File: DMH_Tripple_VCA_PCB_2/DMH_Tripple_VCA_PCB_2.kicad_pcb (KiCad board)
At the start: 2 copper layers, 48 x 175 mm, 0 parts

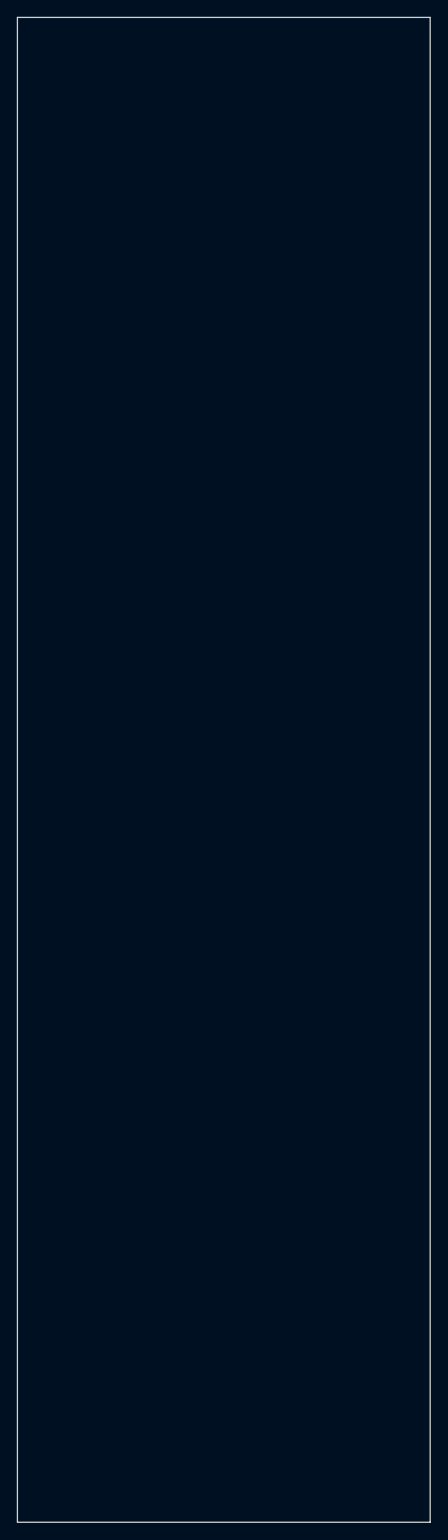
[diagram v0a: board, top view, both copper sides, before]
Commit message: Corrected header locations and placed pcb2 comps
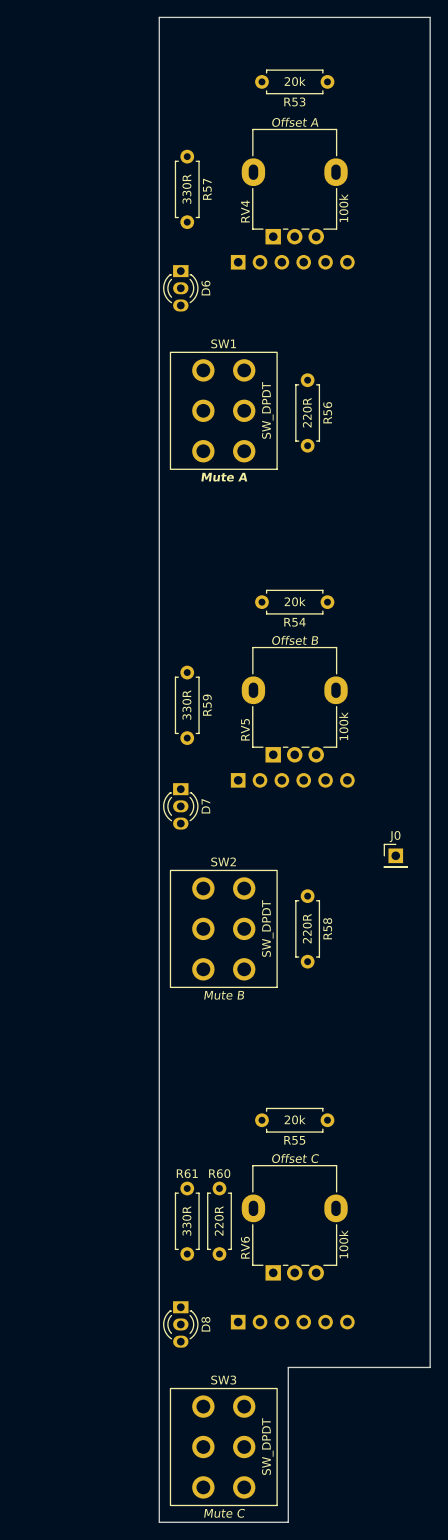
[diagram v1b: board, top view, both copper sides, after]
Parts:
- added D6: LED_Dual_AKA, SynthStuff:LED_D3.0mm-2color, F.Cu at (70.0, 74.0)
- added D7: LED_Dual_AKA, SynthStuff:LED_D3.0mm-2color, F.Cu at (70.0, 134.2)
- added D8: LED_Dual_AKA, SynthStuff:LED_D3.0mm-2color, F.Cu at (70.0, 194.5)
- added J0: Conn_01x01, Connector_PinHeader_2.54mm:PinHeader_1x01_P2.54mm_Vertical, F.Cu at (95.0, 140.0)
- added J50: Conn_01x06, Connector_PinHeader_2.54mm:PinHeader_1x06_P2.54mm_Vertical, B.Cu at (76.7, 71.0)
- added J60: Conn_01x06, Connector_PinHeader_2.54mm:PinHeader_1x06_P2.54mm_Vertical, B.Cu at (76.7, 131.2)
- added J70: Conn_01x06, Connector_PinHeader_2.54mm:PinHeader_1x06_P2.54mm_Vertical, B.Cu at (76.7, 194.2)
- added R53: 20k, Resistor_THT:R_Axial_DIN0207_L6.3mm_D2.5mm_P7.62mm_Horizontal, F.Cu at (87.1, 50.0)
- added R54: 20k, Resistor_THT:R_Axial_DIN0207_L6.3mm_D2.5mm_P7.62mm_Horizontal, F.Cu at (87.1, 110.5)
- added R55: 20k, Resistor_THT:R_Axial_DIN0207_L6.3mm_D2.5mm_P7.62mm_Horizontal, F.Cu at (87.1, 170.8)
- added R56: 220R, Resistor_THT:R_Axial_DIN0207_L6.3mm_D2.5mm_P7.62mm_Horizontal, F.Cu at (84.8, 84.7)
- added R57: 330R, Resistor_THT:R_Axial_DIN0207_L6.3mm_D2.5mm_P7.62mm_Horizontal, F.Cu at (70.8, 58.7)
- added R58: 220R, Resistor_THT:R_Axial_DIN0207_L6.3mm_D2.5mm_P7.62mm_Horizontal, F.Cu at (84.8, 144.7)
- added R59: 330R, Resistor_THT:R_Axial_DIN0207_L6.3mm_D2.5mm_P7.62mm_Horizontal, F.Cu at (70.8, 118.7)
- added R60: 220R, Resistor_THT:R_Axial_DIN0207_L6.3mm_D2.5mm_P7.62mm_Horizontal, F.Cu at (74.5, 178.7)
- added R61: 330R, Resistor_THT:R_Axial_DIN0207_L6.3mm_D2.5mm_P7.62mm_Horizontal, F.Cu at (70.8, 178.7)
- added RV4: 100k, SynthStuff:Potentiometer_Alpha_RD901F-40-00D_Single_Vertical, F.Cu at (80.8, 68.0)
- added RV5: 100k, SynthStuff:Potentiometer_Alpha_RD901F-40-00D_Single_Vertical, F.Cu at (80.8, 128.2)
- added RV6: 100k, SynthStuff:Potentiometer_Alpha_RD901F-40-00D_Single_Vertical, F.Cu at (80.8, 188.5)
- added SW1: SW_DPDT, SynthStuff:Toggle_Switch_2_Poles_THT, F.Cu at (75.0, 88.2)
- added SW2: SW_DPDT, SynthStuff:Toggle_Switch_2_Poles_THT, F.Cu at (75.0, 148.5)
- added SW3: SW_DPDT, SynthStuff:Toggle_Switch_2_Poles_THT, F.Cu at (75.0, 208.8)
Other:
- board size 48 x 175 mm -> 31.5 x 175 mm

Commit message: Routed PCB 2
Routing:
- net +12V: track 0.00 -> 173.6 mm
- net Net-(R60-Pad2): track 0.00 -> 29.2 mm
- net Net-(R53-Pad1): track 0.00 -> 20.6 mm
- net Net-(D8-A2): track 0.00 -> 20.6 mm
- net Net-(R55-Pad1): track 0.00 -> 20.4 mm
- net Net-(R54-Pad1): track 0.00 -> 20.4 mm
- net /Inputs and Outputs/Output B Jack: track 0.00 -> 19.1 mm
- net /Inputs and Outputs/Output A Jack: track 0.00 -> 19.1 mm
- net Net-(R61-Pad2): track 0.00 -> 18.5 mm
- net Net-(D6-A2): track 0.00 -> 18.3 mm
- net Net-(R59-Pad2): track 0.00 -> 18.3 mm
- net Net-(D7-A2): track 0.00 -> 18.2 mm
- net Net-(R57-Pad2): track 0.00 -> 18.0 mm
- net /Inputs and Outputs/Output C Jack: track 0.00 -> 16.3 mm
- net Net-(D8-A1): track 0.00 -> 14.5 mm
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- added copper zone on B.Cu, net GND
- added copper zone on F.Cu, net GND

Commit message: Generated Gerbers
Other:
- board text added: "Mk1.0 - March 2025"
- board text removed: "Mk1.0 - Month Year"
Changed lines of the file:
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@@
 			(plot_on_all_layers_selection 0x00000000_00000000_00000000_00000000)
 			(disableapertmacros no)
-			(usegerberextensions no)
+			(usegerberextensions yes)
 			(usegerberattributes yes)
 			(usegerberadvancedattributes yes)
@@
 			(sketchdnponfab yes)
 			(crossoutdnponfab yes)
-			(subtractmaskfromsilk no)
+			(subtractmaskfromsilk yes)
 			(outputformat 1)
 			(mirror no)
-			(drillshape 1)
+			(drillshape 0)
 			(scaleselection 1)
-			(outputdirectory "")
+			(outputdirectory "Gerbers/")
 		)
 	)
@@
 	)
 	(gr_rect
-		(start 94 186.25)
-		(end 96 196.25)
+		(start 94 186)
+		(end 96 196)
 		(stroke
 			(width 0.1)
@@
 		(layer "User.9")
 	)
-	(gr_text "Mk1.0 - Month Year"
-		(at 97.75 191.25 90)
+	(gr_text "Mk1.0 - March 2025"
+		(at 97.75 191 90)
 		(layer "B.SilkS")
 		(effects

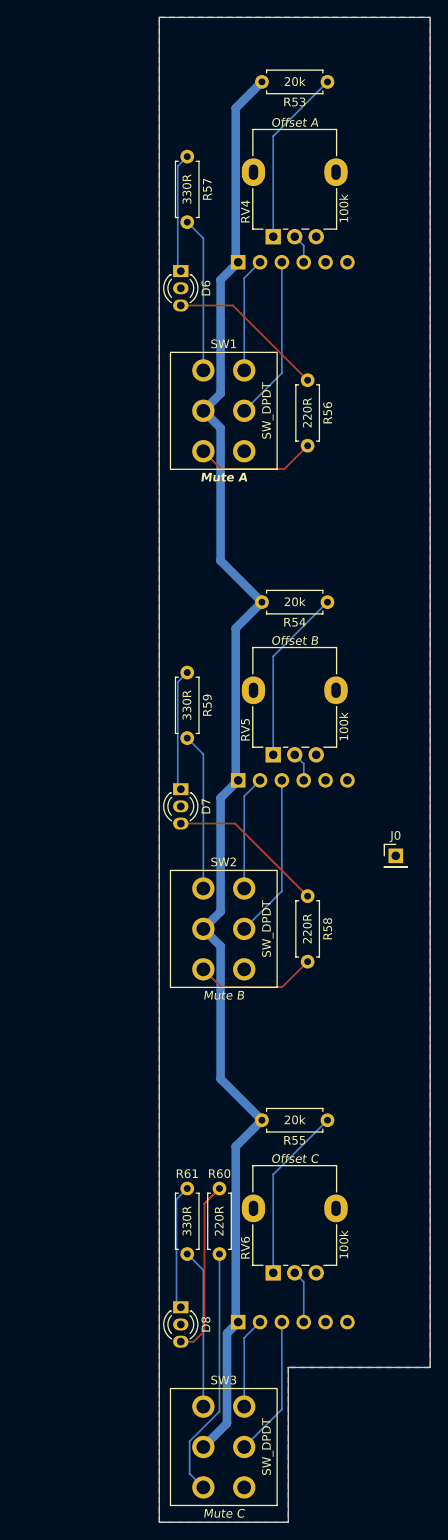
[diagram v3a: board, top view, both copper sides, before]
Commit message: Fixed mistakes in PCB 2
- Inverted offset potentiometers pinout
- LED resistors were too low, changed to 1k both colors
- Regenerated PCB 2 gerbers accordingly
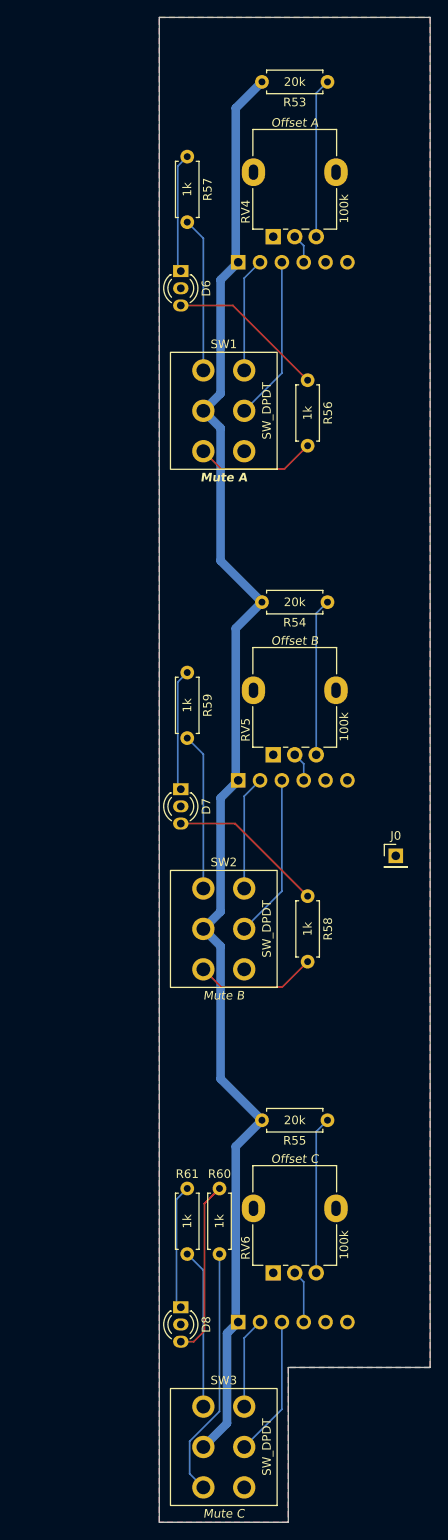
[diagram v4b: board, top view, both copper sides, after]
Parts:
- R56, R58, R60: value 220R -> 1k
- R57, R59, R61: value 330R -> 1k
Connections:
- RV4 pad 1: Net-(R53-Pad1) -> GND
- RV4 pad 3: GND -> Net-(R53-Pad1)
- RV5 pad 1: Net-(R54-Pad1) -> GND
- RV5 pad 3: GND -> Net-(R54-Pad1)
- RV6 pad 1: Net-(R55-Pad1) -> GND
- RV6 pad 3: GND -> Net-(R55-Pad1)
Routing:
- net Net-(R55-Pad1): track 20.4 -> 18.3 mm
- net Net-(R54-Pad1): track 20.4 -> 18.3 mm
- net Net-(R53-Pad1): track 20.6 -> 18.5 mm
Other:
- board text added: "Mk1.1 - March 2025"
- board text removed: "Mk1.0 - March 2025"
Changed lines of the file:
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@@
 			(layers "*.Cu" "*.Mask")
 			(remove_unused_layers no)
-			(net 20 "Net-(R55-Pad1)")
+			(net 3 "GND")
 			(pinfunction "1")
 			(pintype "passive")
@@
 			(layers "*.Cu" "*.Mask")
 			(remove_unused_layers no)
-			(net 3 "GND")
+			(net 20 "Net-(R55-Pad1)")
 			(pinfunction "3")
 			(pintype "passive")
@@
 			)
 		)
-		(property "Value" "330R"
+		(property "Value" "1k"
 			(at 3.81 0 90)
 			(layer "F.SilkS")
@@
 			)
 		)
-		(property "Value" "330R"
+		(property "Value" "1k"
 			(at 3.81 0 90)
 			(layer "F.SilkS")
@@
 			)
 		)
+		(property "Function" ""
+			(at 0 0 270)
+			(unlocked yes)
+			(layer "F.Fab")
+			(hide yes)
+			(effects
+				(font
+					(size 1 1)
+					(thickness 0.15)
+				)
+			)
+		)
 		(property ki_fp_filters "R_*")
 		(sheetname "/Inputs and Outputs/")
@@
 			)
 		)
-		(property "Value" "220R"
+		(property "Value" "1k"
 			(at 3.81 0 90)
 			(layer "F.SilkS")
@@
 			)
 		)
+		(property "Function" ""
+			(at 0 0 270)
+			(unlocked yes)
+			(layer "F.Fab")
+			(hide yes)
+			(effects
+				(font
+					(size 1 1)
+					(thickness 0.15)
+				)
+			)
+		)
 		(property ki_fp_filters "R_*")
 		(sheetname "/Inputs and Outputs/")
@@
 			(layers "*.Cu" "*.Mask")
 			(remove_unused_layers no)
-			(net 18 "Net-(R53-Pad1)")
+			(net 3 "GND")
 			(pinfunction "1")
 			(pintype "passive")
@@
 			(layers "*.Cu" "*.Mask")
 			(remove_unused_layers no)
-			(net 3 "GND")
+			(net 18 "Net-(R53-Pad1)")
 			(pinfunction "3")
 			(pintype "passive")
@@
 			)
 		)
-		(property "Value" "330R"
+		(property "Value" "1k"
 			(at 3.81 0 90)
 			(layer "F.SilkS")
@@
 			)
 		)
+		(property "Function" ""
+			(at 0 0 270)
+			(unlocked yes)
+			(layer "F.Fab")
+			(hide yes)
+			(effects
+				(font
+					(size 1 1)
+					(thickness 0.15)
+				)
+			)
+		)
 		(property ki_fp_filters "R_*")
 		(sheetname "/Inputs and Outputs/")
@@
 			)
 		)
-		(property "Value" "220R"
+		(property "Value" "1k"
 			(at 3.81 0 90)
 			(layer "F.SilkS")
@@
 			)
 		)
+		(property "Function" ""
+			(at 0 0 270)
+			(unlocked yes)
+			(layer "F.Fab")
+			(hide yes)
+			(effects
+				(font
+					(size 1 1)
+					(thickness 0.15)
+				)
+			)
+		)
 		(property ki_fp_filters "R_*")
 		(sheetname "/Inputs and Outputs/")
@@
 			(layers "*.Cu" "*.Mask")
 			(remove_unused_layers no)
-			(net 19 "Net-(R54-Pad1)")
+			(net 3 "GND")
 			(pinfunction "1")
 			(pintype "passive")
@@
 			(layers "*.Cu" "*.Mask")
 			(remove_unused_layers no)
-			(net 3 "GND")
+			(net 19 "Net-(R54-Pad1)")
 			(pinfunction "3")
 			(pintype "passive")
@@
 			)
 		)
-		(property "Value" "220R"
+		(property "Value" "1k"
 			(at 3.81 0 90)
 			(layer "F.SilkS")
@@
 			)
 		)
+		(property "Function" ""
+			(at 0 0 270)
+			(unlocked yes)
+			(layer "F.Fab")
+			(hide yes)
+			(effects
+				(font
+					(size 1 1)
+					(thickness 0.15)
+				)
+			)
+		)
 		(property ki_fp_filters "R_*")
 		(sheetname "/Inputs and Outputs/")
@@
 		(layer "User.9")
 	)
-	(gr_text "Mk1.0 - March 2025"
+	(gr_text "Mk1.1 - March 2025"
 		(at 97.75 191 90)
 		(layer "B.SilkS")
@@
 	)
 	(segment
-		(start 87.06 50)
-		(end 80.75 56.31)
+		(start 85.75 51.31)
+		(end 87.06 50)
 		(width 0.2)
 		(layer "B.Cu")
@@
 	)
 	(segment
-		(start 80.75 56.31)
-		(end 80.75 68)
+		(start 85.75 68)
+		(end 85.75 51.31)
 		(width 0.2)
 		(layer "B.Cu")
@@
 	(segment
 		(start 87.06 110.5)
-		(end 80.75 116.81)
+		(end 85.75 111.81)
 		(width 0.2)
 		(layer "B.Cu")
@@
 	)
 	(segment
-		(start 80.75 116.81)
-		(end 80.75 128.25)
+		(start 85.75 111.81)
+		(end 85.75 128.25)
 		(width 0.2)
 		(layer "B.Cu")
@@
 	)
 	(segment
-		(start 80.75 177.06)
-		(end 80.75 188.5)
+		(start 85.75 172.06)
+		(end 87.06 170.75)
 		(width 0.2)
 		(layer "B.Cu")
@@
 	)
 	(segment
-		(start 87.06 170.75)
-		(end 80.75 177.06)
+		(start 85.75 188.5)
+		(end 85.75 172.06)
 		(width 0.2)
 		(layer "B.Cu")
